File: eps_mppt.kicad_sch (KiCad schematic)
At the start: 24 parts, among them J1 PV_IN, J2 OUT, U1 SPV1040, U2 ACS725xLCTR-10AU, U3 ADS7830

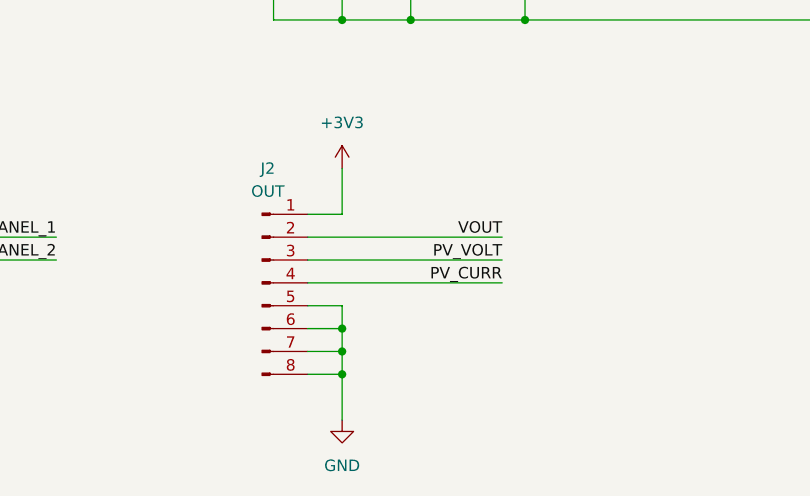
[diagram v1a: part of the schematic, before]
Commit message: Optimized layout, truncated board
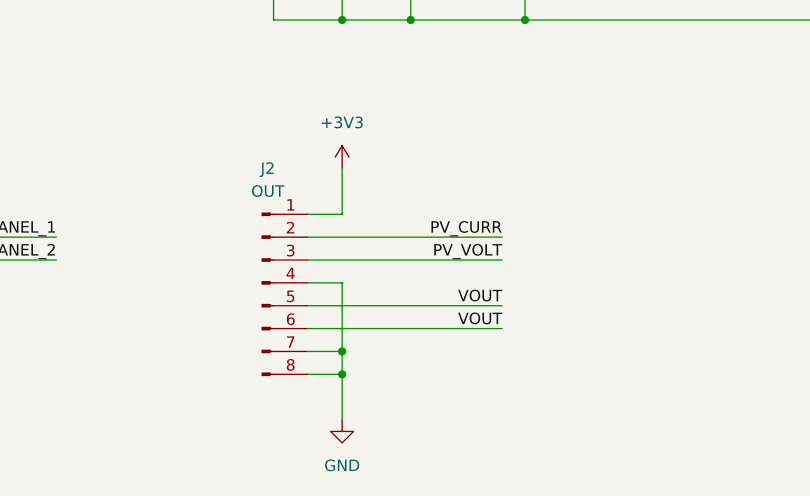
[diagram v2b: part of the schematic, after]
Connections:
- net GND: now also J2.4 (Pin_4); no longer J2.5 (Pin_5), J2.6 (Pin_6)
- net PV_CURR: now also J2.2 (Pin_2); no longer J2.4 (Pin_4)
- net VOUT: now also J2.5 (Pin_5), J2.6 (Pin_6); no longer J2.2 (Pin_2)
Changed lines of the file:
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@@
+	)
+	(junction
+		(at 114.3 99.06)
+		(diameter 0)
+		(color 0 0 0 0)
+	)
+	(junction
+		(at 106.68 85.09)
+		(diameter 0)
+		(color 0 0 0 0)
+	)
+	(junction
+		(at 232.41 60.96)
+		(diameter 0)
+		(color 0 0 0 0)
 	)
 	(junction
@@
 	)
 	(junction
-		(at 114.3 99.06)
-		(diameter 0)
-		(color 0 0 0 0)
-	)
-	(junction
-		(at 106.68 85.09)
-		(diameter 0)
-		(color 0 0 0 0)
-	)
-	(junction
-		(at 232.41 60.96)
-		(diameter 0)
-		(color 0 0 0 0)
-	)
-	(junction
-		(at 106.68 157.48)
-		(diameter 0)
-		(color 0 0 0 0)
-	)
-	(junction
 		(at 180.34 99.06)
 		(diameter 0)
@@
 	(wire
 		(pts
-			(xy 106.68 154.94) (xy 106.68 157.48)
-		)
-		(stroke
-			(width 0)
-			(type default)
-		)
-	)
-	(wire
-		(pts
 			(xy 49.53 99.06) (xy 64.77 99.06)
 		)
@@
 	(wire
 		(pts
+			(xy 106.68 152.4) (xy 106.68 160.02)
+		)
+		(stroke
+			(width 0)
+			(type default)
+		)
+	)
+	(wire
+		(pts
 			(xy 100.33 78.74) (xy 100.33 85.09)
 		)
@@
 	(wire
 		(pts
-			(xy 102.87 154.94) (xy 106.68 154.94)
-		)
-		(stroke
-			(width 0)
-			(type default)
-		)
-	)
-	(wire
-		(pts
-			(xy 102.87 152.4) (xy 124.46 152.4)
+			(xy 102.87 154.94) (xy 124.46 154.94)
 		)
 		(stroke
@@
 	(wire
 		(pts
-			(xy 102.87 157.48) (xy 106.68 157.48)
+			(xy 102.87 157.48) (xy 124.46 157.48)
 		)
 		(stroke
@@
 	(wire
 		(pts
-			(xy 106.68 157.48) (xy 106.68 160.02)
-		)
-		(stroke
-			(width 0)
-			(type default)
-		)
-	)
-	(wire
-		(pts
 			(xy 180.34 85.09) (xy 180.34 99.06)
 		)
@@
 		(pts
 			(xy 49.53 109.22) (xy 49.53 111.76)
+		)
+		(stroke
+			(width 0)
+			(type default)
+		)
+	)
+	(wire
+		(pts
+			(xy 102.87 152.4) (xy 106.68 152.4)
 		)
 		(stroke
@@
 	)
 	(label "VOUT"
-		(at 124.46 147.32 180)
+		(at 124.46 154.94 180)
 		(fields_autoplaced yes)
 		(effects
@@
 		)
 	)
+	(label "VOUT"
+		(at 124.46 157.48 180)
+		(fields_autoplaced yes)
+		(effects
+			(font
+				(size 1.27 1.27)
+			)
+			(justify right bottom)
+		)
+	)
 	(label "PANEL_2"
 		(at 64.77 111.76 0)
@@
 	)
 	(label "PV_CURR"
-		(at 124.46 152.4 180)
+		(at 124.46 147.32 180)
 		(fields_autoplaced yes)
 		(effects
